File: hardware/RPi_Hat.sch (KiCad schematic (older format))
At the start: 9 parts, among them J1 RPi_GPIO

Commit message: Almost finished schematic
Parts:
- removed P?: CONN_2, symbol CONN_2
- added C?: C, symbol C
- added CON?: BARREL_JACK, symbol BARREL_JACK
- added D? (x7): ZENER, symbol ZENER
- added D? (x3): DIODESCH, symbol DIODESCH
- added D? (x2): LED, symbol LED
- added P? (x4): CONN_2, symbol CONN_2
- added Q? (x7): DMP3056L-7, symbol MOSFET_P
- added Q? (x4): NPN, symbol NPN
- added R? (x5): 100K, symbol R
- added R? (x5): R, symbol R
- added R? (x5): 500K, symbol R
- added R? (x6): 47K, symbol R
- added R? (x4): 10K, symbol R
- added R? (x4): 1K, symbol R
- added R?: 5m, symbol R
- added RV?: POT, symbol POT
- added S? (x2): BUCKCNV, symbol BUCKCNV
- added S?: BUCKCNV-CC, symbol BUCKCNV
- added U? (x3): DMMT5401, symbol DMMT5401
- added U?: MAX44284, symbol MAX44284
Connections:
- net labels added: AUX1, AUX2, EN_AUXOUT, EN_BATT, EN_BATTMON, EN_CHG, EN_CURRMON, LED_GREEN, LED_RED, PBUS_IN, S_AUXOUT, S_BATT, S_CURRENT, S_PBUS, S_PBUSCMP
- net labels removed: S_RAIL
- wire segments 63 -> 236
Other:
- note added: "BC847A - Hfe: 170"
- moved on the sheet: C?, D?, IC?, J1, P?, U?

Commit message: Semi finished pcb
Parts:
- removed CON?: BARREL_JACK, symbol BARREL_JACK
- removed D?: ZENER, symbol ZENER
- removed P?: DIL6, symbol DIL6
- removed Q?: DMP3056L-7, symbol MOSFET_P
- removed Q?: NPN, symbol NPN
- removed R? (x2): 100K, symbol R
- removed R?: R, symbol R
- added C1, C11, C2, C3, C6, C7, C9: 2n, Capacitors_SMD:C_0805_HandSoldering, symbol C
- added C12, C13, C14: CP, Capacitors_THT:CP_Radial_D8.0mm_P3.50mm, symbol CP
- added P4: CONN_2, Connectors_Molex:Molex_KK-6410-02_02x2.54mm_Straight, symbol CONN_2
- added P6: Conn_02x03_Odd_Even, extras:Header_2x03, symbol Conn_02x03_Odd_Even
- added Q10: BC846BPDW1, TO_SOT_Packages_SMD:SOT-363_SC-70-6_Handsoldering, symbol BC846BPDW1
- added R31: 10K, Resistors_SMD:R_0805_HandSoldering, symbol R
- added R32: 1K, Resistors_SMD:R_0805_HandSoldering, symbol R
- C4, C5: renamed from C?; value C -> 10n; footprint (none) -> Capacitors_SMD:C_0805_HandSoldering
- C8: renamed from C?; footprint (none) -> Capacitors_SMD:C_0805_HandSoldering
- D1, D10, D2, D3, D8: renamed from D?; footprint (none) -> Diodes_SMD:D_SMA_Handsoldering
- D11, D12: renamed from D?; footprint (none) -> Diodes_SMD:D_0805
- D13, D4, D5, D6, D7, D9: renamed from D?; footprint (none) -> Diodes_SMD:D_SOD-123F
- IC1: renamed from IC?; footprint SO20 -> Housings_SOIC:SO-20_12.8x7.5mm_Pitch1.27mm
- P1, P2, P3, P5: renamed from P?; footprint (none) -> Connectors_Molex:Molex_KK-6410-02_02x2.54mm_Straight
- Q1, Q2, Q3, Q4, Q5, Q6, Q7, Q8, Q9: renamed from Q?; footprint (none) -> TO_SOT_Packages_SMD:SOT-23_Handsoldering
- R10, R11, R12, R13, R14, R15, R16, R17, R19, R2, R20, R22, R23, R24, R25, R26, R27, R3, R30, R4, R5, R6, R7, R8, R9: renamed from R?; footprint (none) -> Resistors_SMD:R_0805_HandSoldering
- R18, R21: renamed from R?; value R -> 220R; footprint (none) -> Resistors_SMD:R_0805_HandSoldering
- RV1: renamed from RV?; footprint (none) -> Potentiometers:Potentiometer_Trimmer_Bourns_PV36W
- S1, S2: renamed from S?; footprint (none) -> extras:BUCK
- S3: renamed from S?; footprint (none) -> Connectors_Molex:Molex_KK-6410-04_04x2.54mm_Straight
- U1, U2, U3, U5: renamed from U?; footprint (none) -> TO_SOT_Packages_SMD:SOT-23-6_Handsoldering
- U4: renamed from U?; footprint (none) -> TO_SOT_Packages_SMD:SOT-23-5_HandSoldering
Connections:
- net labels removed: S_BAT
- wire segments 236 -> 274
- no-connect marks 1 -> 29
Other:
- note removed: "BC847A - Hfe: 170"
- moved on the sheet: D11, D12, D9, P5, Q6, Q7, R17, R22, R26, R27, R30, R5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

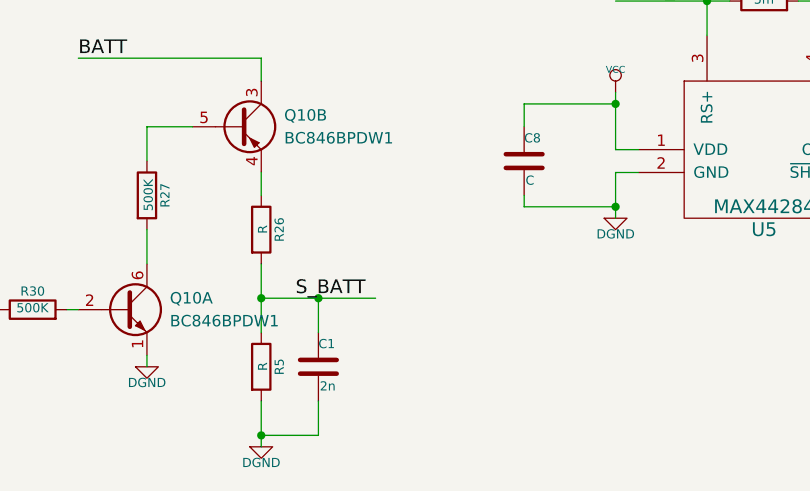
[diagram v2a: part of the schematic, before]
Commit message: BOM Updates for Rev1
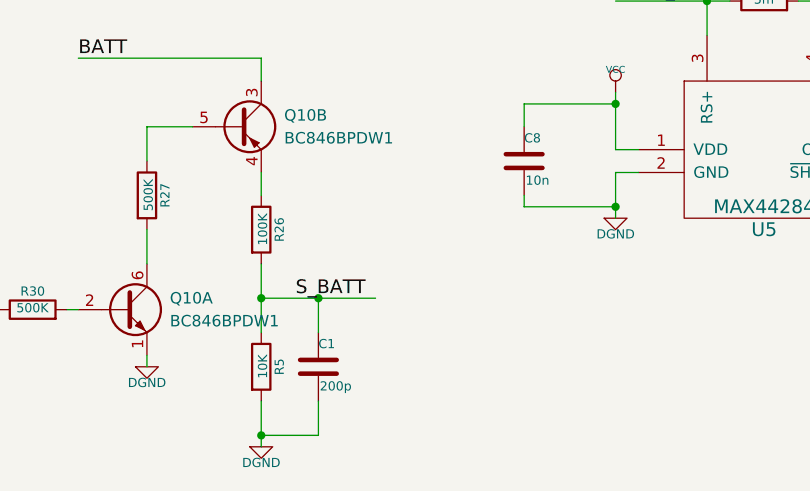
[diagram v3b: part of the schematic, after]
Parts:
- C1: value 2n -> 200p
- C8: value C -> 10n
- R26: value R -> 100K
- R5: value R -> 10K
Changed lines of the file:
@@
 P 5650 9150
 F 0 "R26" V 5730 9150 40  0000 C CNN
-F 1 "R" V 5657 9151 40  0000 C CNN
+F 1 "100K" V 5657 9151 40  0000 C CNN
 F 2 "Resistors_SMD:R_0805_HandSoldering" V 5580 9150 30  0001 C CNN
 F 3 "" H 5650 9150 30  0000 C CNN
@@
 P 5650 9750
 F 0 "R5" V 5730 9750 40  0000 C CNN
-F 1 "R" V 5657 9751 40  0000 C CNN
+F 1 "10K" V 5657 9751 40  0000 C CNN
 F 2 "Resistors_SMD:R_0805_HandSoldering" V 5580 9750 30  0001 C CNN
 F 3 "" H 5650 9750 30  0000 C CNN
@@
 P 6800 8850
 F 0 "C8" H 6800 8950 40  0000 L CNN
-F 1 "C" H 6806 8765 40  0000 L CNN
+F 1 "10n" H 6806 8765 40  0000 L CNN
 F 2 "Capacitors_SMD:C_0805_HandSoldering" H 6838 8700 30  0001 C CNN
 F 3 "" H 6800 8850 60  0000 C CNN
@@
 P 5900 9750
 F 0 "C1" H 5900 9850 40  0000 L CNN
-F 1 "2n" H 5906 9665 40  0000 L CNN
+F 1 "200p" H 5906 9665 40  0000 L CNN
 F 2 "Capacitors_SMD:C_0805_HandSoldering" H 5938 9600 30  0001 C CNN
 F 3 "" H 5900 9750 60  0000 C CNN
